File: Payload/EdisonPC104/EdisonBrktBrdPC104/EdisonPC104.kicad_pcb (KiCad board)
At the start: 2 copper layers, 96 x 92 mm, 10 parts, among them J17 CONN_14, J18 CONN_14, J19 CONN_14, J20 CONN_14, K1 CONN_3, K2 CONN_3, U1 ADG3308, U2 ADG3308

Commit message: se crea nueva version de placa para alojar Rasp Zero y Edison. Se parte con arreglar los errores detectados en la parte de Edison
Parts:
- removed K1, K2: CONN_3, Pin_Headers:Pin_Header_Straight_1x03
- removed U1: ADG3308, Housings_SSOP:TSSOP-20_4.4x6.5mm_Pitch0.65mm
- added 10k1: R, Resistors_SMD:R_1206_HandSoldering, F.Cu at (106.3, 155.3)
- added 10k2: R, Resistors_SMD:R_1206_HandSoldering, F.Cu at (106.5, 162.0)
- added 10k3: R, Resistors_SMD:R_1206_HandSoldering, F.Cu at (114.3, 155.2)
- added 10k4: R, Resistors_SMD:R_1206_HandSoldering, F.Cu at (114.4, 162.1)
- added 10uF1: C, SMD_Packages:SMD-1206_Pol, F.Cu at (122.2, 161.9)
- added 200k1: R, Resistors_SMD:R_1206_HandSoldering, F.Cu at (122.0, 155.3)
- added K3: CONN_3, Pin_Headers:Pin_Header_Straight_1x03, F.Cu at (101.6, 134.6)
- added P1: CONN_01X06, Pin_Headers:Pin_Header_Angled_1x06, F.Cu at (112.1, 177.1)
- added P2: CONN_01X06, Pin_Headers:Pin_Header_Angled_1x06, F.Cu at (97.5, 177.1)
- added R1: R, Resistors_ThroughHole:Resistor_Horizontal_RM15mm, F.Cu at (132.3, 189.4)
- added U3: SN74LVC1T45, TO_SOT_Packages_SMD:SOT-23-6, F.Cu at (140.4, 161.9)
- added U4: SN74LVC1T45, TO_SOT_Packages_SMD:SOT-23-6, F.Cu at (139.9, 154.7)
- added U5: SN74LVC1T45, TO_SOT_Packages_SMD:SOT-23-6, F.Cu at (151.2, 154.2)
- added U6: SN74LVC1T45, TO_SOT_Packages_SMD:SOT-23-6, F.Cu at (152.2, 161.8)
- U2: value ADG3308 -> PCA9306; footprint Housings_SSOP:TSSOP-20_4.4x6.5mm_Pitch0.65mm -> SMD_Packages:SOIC-8-N
- moved U2 47.8 mm to (91.5, 159.5)
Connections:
- net /5V_SYS renamed +5V
- H1 pad 17: /URX1 -> Net-(H1-Pad17)
- H1 pad 18: /UTX1 -> Net-(H1-Pad18)
- H1 pad 19: /URX0 -> Net-(H1-Pad19)
- H1 pad 20: /UTX0 -> Net-(H1-Pad20)
- H1 pad 21: /SCK0 -> Net-(H1-Pad21)
- H1 pad 22: /SDI0 -> Net-(H1-Pad22)
- H1 pad 23: /SDO0 -> Net-(H1-Pad23)
- H1 pad 24: /nCS_SD -> Net-(H1-Pad24)
- J20 pad 1: +3V3 -> /V_VSYS
- U2 pad 1: +1.8V -> GND
- U2 pad 2: Net-(U2-Pad2) -> +1.8V
- U2 pad 3: Net-(U2-Pad3) -> /GP19_I2C1_SCL
- U2 pad 4: Net-(U2-Pad4) -> /GP20_I2C1_SDA
- U2 pad 5: /GP15 -> /SDA_SYS
- U2 pad 6: /GP110_SSP5_FS0 -> /SCL_SYS
- U2 pad 7: /GP109_SSP5_CLK -> Net-(10uF1-Pad2)
- U2 pad 8: /GP115_SSP5_TXD -> Net-(10uF1-Pad2)
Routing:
- net +3V3: track 144.2 -> 2.54 mm, vias 3 -> 0
- net GND: track 127.7 -> 5.08 mm, vias 2 -> 0
- net +1.8V: track 64.8 -> 0.00 mm, vias 2 -> 0
- net /GP130_UART1_RX: track 57.5 -> 0.00 mm, vias 2 -> 0
- net Net-(H2-Pad9): track 55.9 -> 0.00 mm
- net /SCL_SYS: track 52.9 -> 0.00 mm, vias 1 -> 0
- net /SDA_SYS: track 52.9 -> 0.00 mm, vias 1 -> 0
- net /GP131_UART1_TX: track 49.0 -> 0.06 mm, vias 2 -> 0
- net /SDI0: track 45.5 -> 0.00 mm
- net /nCS_SD: track 41.6 -> 0.00 mm, vias 2 -> 0
- net /SCK0: track 38.1 -> 0.00 mm
- net /SDO0: track 37.3 -> 0.00 mm
- net /UTX0: track 37.2 -> 0.00 mm, vias 2 -> 0
- net /GP20_I2C1_SDA: track 36.7 -> 0.00 mm, vias 2 -> 0
- net /GP134_UART2_RX: track 36.7 -> 0.00 mm, vias 2 -> 0
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
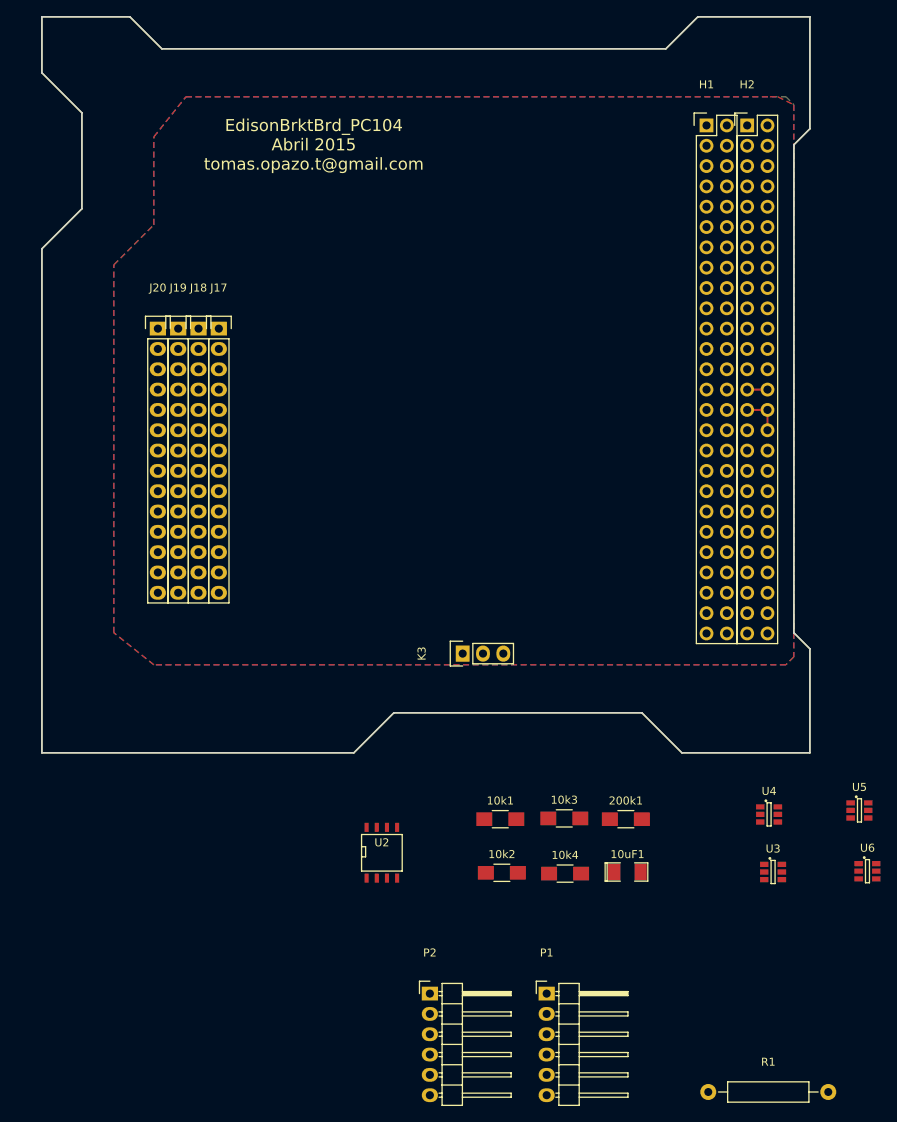
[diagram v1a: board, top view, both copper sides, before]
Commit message: se corrige bug de ruteo de UART1 y 2
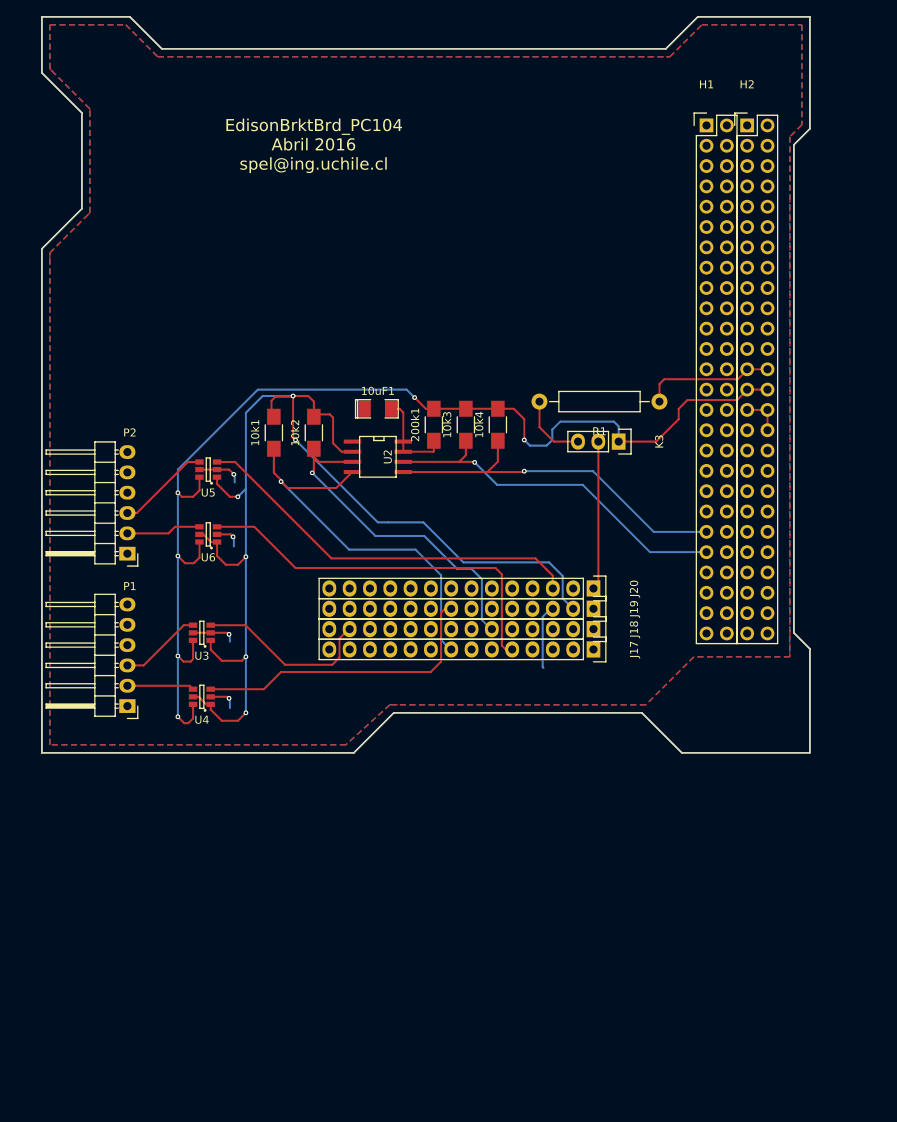
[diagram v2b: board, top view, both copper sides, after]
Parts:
- moved U6 92.5 mm to (69.8, 119.7), turned to 180 degrees
- moved U5 91.9 mm to (69.8, 111.6), turned to 180 degrees
- moved R1 86.5 mm to (126.2, 103.1), turned to 180 degrees
- moved U3 77.4 mm to (69.0, 132.0), turned to 180 degrees
- moved U4 72.4 mm to (69.0, 140.0), turned to 180 degrees
- moved P2 66.7 mm to (59.7, 122.1), turned to 180 degrees
- moved 10uF1 65.8 mm to (91.0, 104.0)
- moved P1 63.5 mm to (59.7, 141.2), turned to 180 degrees
- moved J20 63.4 mm to (118.0, 126.5), turned to 270 degrees
- moved J19 62.6 mm to (118.0, 129.0), turned to 270 degrees
- moved J18 62.0 mm to (118.0, 131.5), turned to 270 degrees
- moved J17 61.7 mm to (118.0, 134.1), turned to 270 degrees
- moved 10k2 59.8 mm to (83.0, 107.0), turned to 90 degrees
- moved 10k4 56.7 mm to (106.0, 106.0), turned to 90 degrees
- moved 10k1 56.0 mm to (78.0, 107.0), turned to 90 degrees
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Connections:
- P1 pad 2: /FTDI_RX -> /FTDI1_RX
- P1 pad 3: /FTDI_TX -> /FTDI1_TX
- P2 pad 2: /FTDI_RX -> /FTDI2_RX
- P2 pad 3: /FTDI_TX -> /FTDI2_TX
- U3 pad 4: /FTDI_TX -> /FTDI1_TX
- U4 pad 3: /GP135_UART2_TX -> /GP131_UART1_TX
- U4 pad 4: /FTDI_RX -> /FTDI1_RX
- U5 pad 4: /FTDI_TX -> /FTDI2_TX
- U6 pad 3: /GP131_UART1_TX -> /GP135_UART2_TX
- U6 pad 4: /FTDI_RX -> /FTDI2_RX
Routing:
- net +1.8V: track 0.00 -> 142.9 mm, vias 0 -> 6
- net +3V3: track 2.54 -> 140.2 mm, vias 0 -> 6
- net /GP134_UART2_RX: track 0.00 -> 49.5 mm
- net /GP20_I2C1_SDA: track 0.00 -> 49.4 mm, vias 0 -> 1
- net /GP135_UART2_TX: track 0.00 -> 48.6 mm
- net /SDA_SYS: track 0.00 -> 45.7 mm, vias 0 -> 1
- net /SCL_SYS: track 0.00 -> 45.6 mm, vias 0 -> 1
- net /GP19_I2C1_SCL: track 0.00 -> 42.7 mm, vias 0 -> 1
- net /GP131_UART1_TX: track 0.06 -> 37.9 mm
- net GND: track 5.08 -> 31.3 mm, vias 0 -> 4
- net /GP130_UART1_RX: track 0.00 -> 22.7 mm
- net /V_VSYS: track 0.00 -> 20.4 mm
- net +5V: track 0.00 -> 16.5 mm
- net Net-(10uF1-Pad2): track 0.00 -> 11.8 mm
- net /FTDI2_TX: track 0.00 -> 11.7 mm
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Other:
- board text added: "EdisonBrktBrd_PC104 Abril 2016 spel@ing.uchile.cl"
- board text added: "footprint for SOT-23-6"
- board text added: "footprint for SOT96-1 (SO8)"
- board text removed: "EdisonBrktBrd_PC104 Abril 2015 tomas.opazo.t@gmail.com"

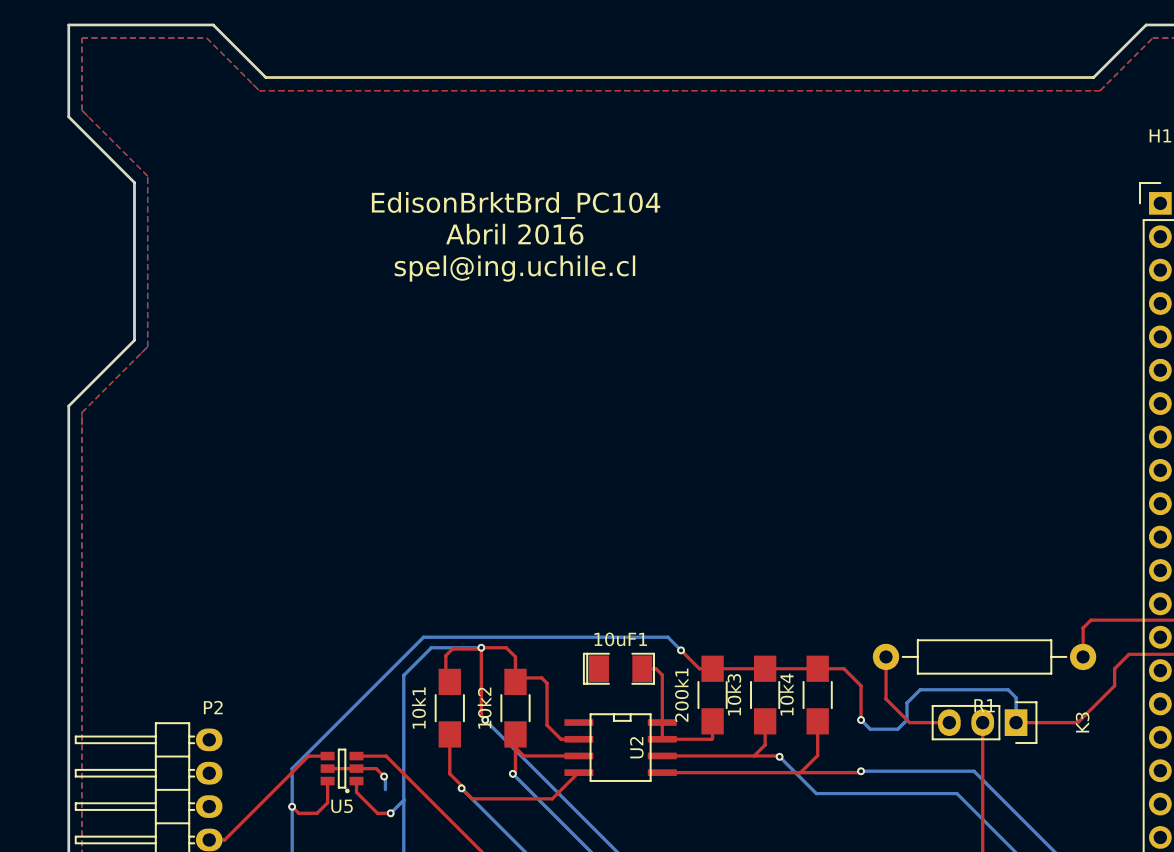
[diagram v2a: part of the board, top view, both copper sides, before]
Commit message: se agrega rapberry zero al PCB
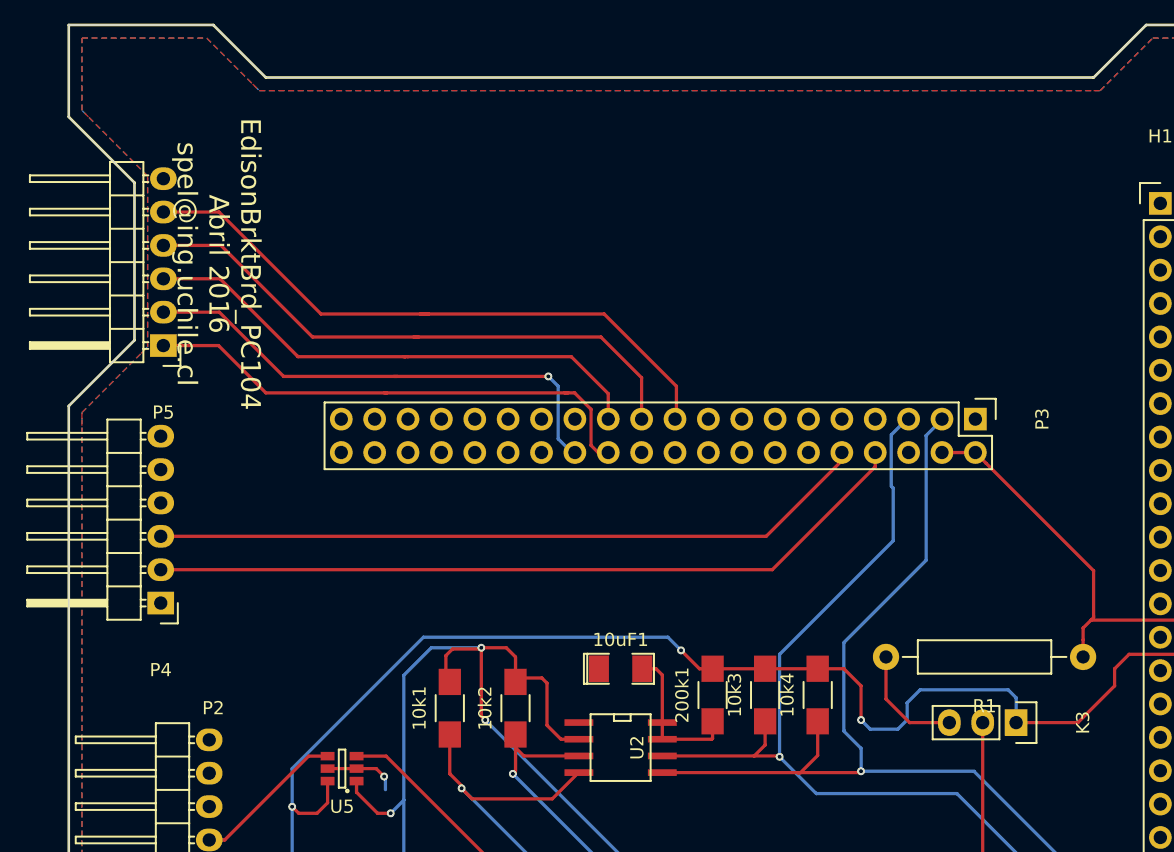
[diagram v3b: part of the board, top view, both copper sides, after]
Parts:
- added P3: CONN_02X20, Pin_Headers:Pin_Header_Straight_2x20, F.Cu at (118.0, 85.0)
- added P4: CONN_01X06, Pin_Headers:Pin_Header_Angled_1x06, F.Cu at (56.0, 99.0)
- added P5: CONN_01X06, Pin_Headers:Pin_Header_Angled_1x06, F.Cu at (56.2, 79.4)
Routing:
- net /FTDI3_RX: track 0.00 -> 58.7 mm
- net /FTDI3_TX: track 0.00 -> 54.8 mm
- net /MOSI: track 0.00 -> 47.7 mm
- net /MISO: track 0.00 -> 44.1 mm
- net /SCLK: track 0.00 -> 39.5 mm
- net /CS0: track 0.00 -> 39.3 mm
- net /CS1: track 0.00 -> 38.3 mm, vias 0 -> 1
- net /SDA_SYS: track 45.7 -> 76.6 mm
- net /SCL_SYS: track 45.6 -> 75.5 mm
- net +5V: track 16.5 -> 35.6 mm
